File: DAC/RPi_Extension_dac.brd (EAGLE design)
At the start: 63 x 50 mm, 33 parts, among them U1 AD5360BSTZ, U2 ADR423ARZ

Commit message: updated pcbs
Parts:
- C1, C10, C12, C13, C15, C16, C2, C6, C8: value (none) -> 100nF
- C11, C14, C17, C3, C4, C5, C7, C9: value (none) -> 10uF
- R1, R2: value (none) -> 100k
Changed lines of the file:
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@@
 <attribute name="OC_FARNELL" value="unknown" x="29.25" y="4.55" size="1.778" layer="27" rot="R180" display="off"/>
 </element>
-<element name="C1" library="rcl" package="C0603" value="" x="17.55" y="28" rot="R270"/>
-<element name="C2" library="rcl" package="C0603" value="" x="25.8" y="28.35"/>
-<element name="C3" library="rcl" package="C1206" value="" x="16.15" y="31.3" rot="R180"/>
-<element name="C4" library="rcl" package="C1206" value="" x="26.35" y="31"/>
-<element name="C5" library="rcl" package="C1206" value="" x="9.1" y="22.75" rot="R90"/>
-<element name="C6" library="rcl" package="C0603" value="" x="11.7" y="22.2" rot="R90"/>
-<element name="C7" library="rcl" package="C1206" value="" x="35.1" y="13.85"/>
-<element name="C8" library="rcl" package="C0603" value="" x="29.9" y="13.65" rot="R270"/>
-<element name="C9" library="rcl" package="C1206" value="" x="9.1" y="16.25" rot="R270"/>
-<element name="C10" library="rcl" package="C0603" value="" x="11.7" y="16.8" rot="R270"/>
-<element name="C11" library="rcl" package="C1206" value="" x="35.1" y="16.9"/>
-<element name="C12" library="rcl" package="C0603" value="" x="29.95" y="17.1" rot="R90"/>
+<element name="C1" library="rcl" package="C0603" value="100nF" x="17.55" y="28" rot="R270"/>
+<element name="C2" library="rcl" package="C0603" value="100nF" x="25.8" y="28.35"/>
+<element name="C3" library="rcl" package="C1206" value="10uF" x="16.15" y="31.3" rot="R180"/>
+<element name="C4" library="rcl" package="C1206" value="10uF" x="26.35" y="31"/>
+<element name="C5" library="rcl" package="C1206" value="10uF" x="9.1" y="22.75" rot="R90"/>
+<element name="C6" library="rcl" package="C0603" value="100nF" x="11.7" y="22.2" rot="R90"/>
+<element name="C7" library="rcl" package="C1206" value="10uF" x="35.1" y="13.85"/>
+<element name="C8" library="rcl" package="C0603" value="100nF" x="29.9" y="13.65" rot="R270"/>
+<element name="C9" library="rcl" package="C1206" value="10uF" x="9.1" y="16.25" rot="R270"/>
+<element name="C10" library="rcl" package="C0603" value="100nF" x="11.7" y="16.8" rot="R270"/>
+<element name="C11" library="rcl" package="C1206" value="10uF" x="35.1" y="16.9"/>
+<element name="C12" library="rcl" package="C0603" value="100nF" x="29.95" y="17.1" rot="R90"/>
 <element name="SV3" library="con-lsta" package="FE08-2" value="" x="4.55" y="17.55" rot="R270">
 <attribute name="MPN" value="" x="4.55" y="17.55" size="1.778" layer="27" rot="R270" display="off"/>
@@
 <attribute name="VENDOR" value="Vendor" x="12.35" y="5.05" size="1.778" layer="27" display="off"/>
 </element>
-<element name="C13" library="rcl" package="C0603" value="" x="6.7" y="4.85" rot="R270"/>
-<element name="C14" library="rcl" package="C1206" value="" x="3.9" y="4.3" rot="R270"/>
-<element name="C15" library="rcl" package="C0603" value="" x="17.55" y="4.2" rot="R270"/>
-<element name="C16" library="rcl" package="C0603" value="" x="12.35" y="12.35" rot="R180"/>
-<element name="C17" library="rcl" package="C1206" value="" x="11.8" y="9.65" rot="R180"/>
+<element name="C13" library="rcl" package="C0603" value="100nF" x="6.7" y="4.85" rot="R270"/>
+<element name="C14" library="rcl" package="C1206" value="10uF" x="3.9" y="4.3" rot="R270"/>
+<element name="C15" library="rcl" package="C0603" value="100nF" x="17.55" y="4.2" rot="R270"/>
+<element name="C16" library="rcl" package="C0603" value="100nF" x="12.35" y="12.35" rot="R180"/>
+<element name="C17" library="rcl" package="C1206" value="10uF" x="11.8" y="9.65" rot="R180"/>
 <element name="SV2" library="con-lstb" package="MA08-2W" value="" x="51.35" y="4.55" rot="R180">
 <attribute name="MF" value="" x="51.35" y="4.55" size="1.778" layer="27" rot="R180" display="off"/>
@@
 <element name="SJ7" library="jumper" package="SJ" value="" x="8.45" y="35.1" rot="R270"/>
 <element name="SJ8" library="jumper" package="SJ" value="" x="4.55" y="35.1" rot="R270"/>
-<element name="R1" library="resistor" package="R0603" value="" x="12.2" y="25.05"/>
-<element name="R2" library="resistor" package="R0603" value="" x="12.2" y="27.6"/>
+<element name="R1" library="resistor" package="R0603" value="100k" x="12.2" y="25.05"/>
+<element name="R2" library="resistor" package="R0603" value="100k" x="12.2" y="27.6"/>
 </elements>
 <signals>

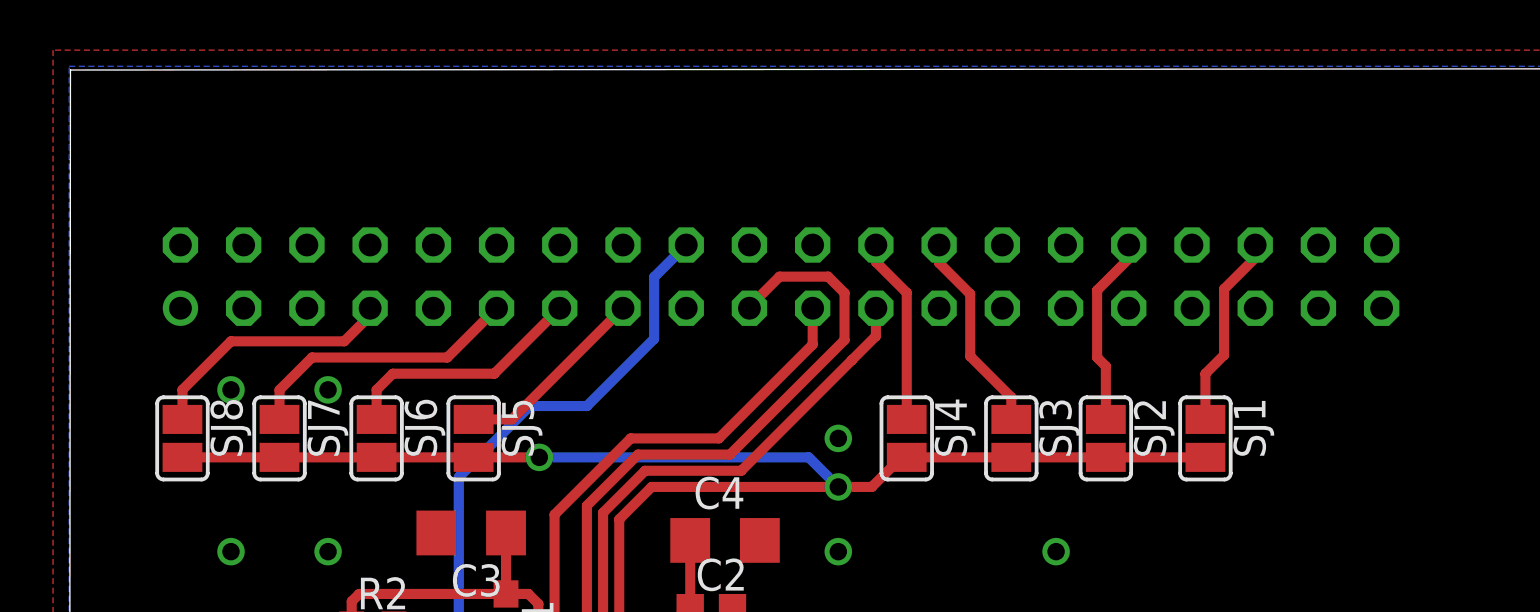
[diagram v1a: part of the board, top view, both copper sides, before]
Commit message: added additional id jumpers to adc and dac board
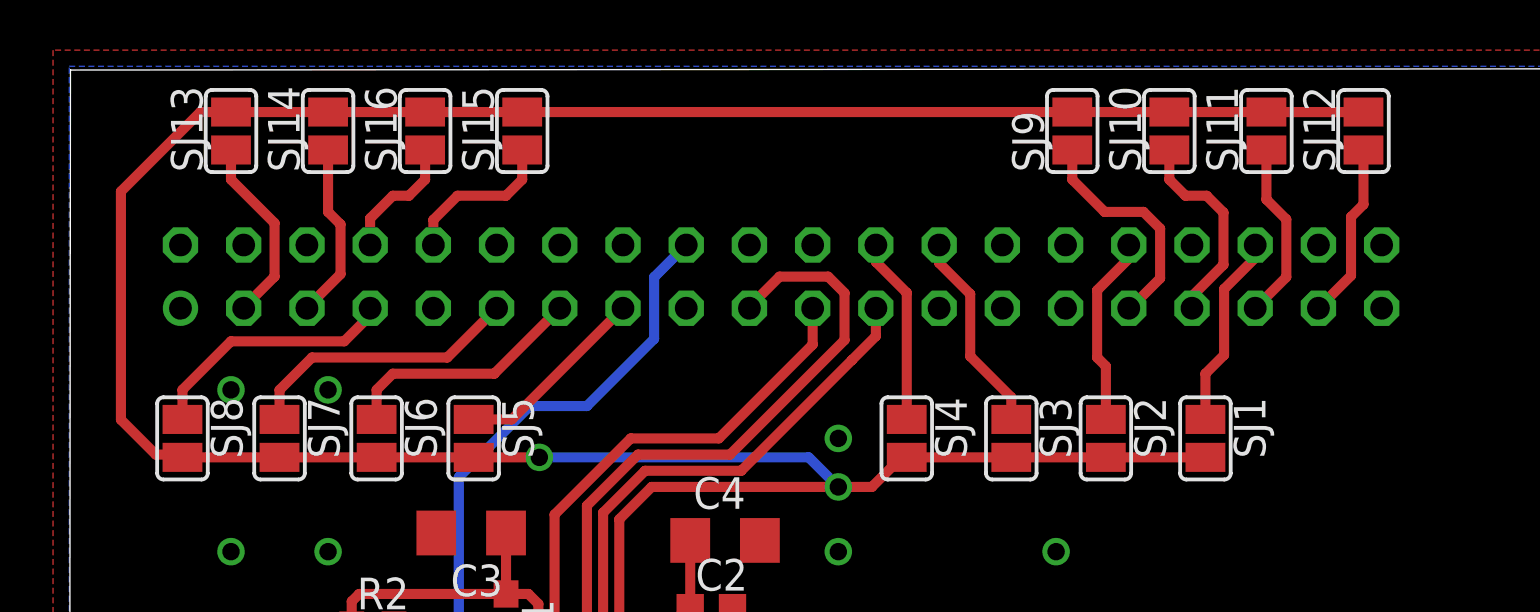
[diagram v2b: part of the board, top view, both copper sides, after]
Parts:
- added SJ10, SJ11, SJ12, SJ13, SJ14, SJ15, SJ16, SJ9: (no value), jumper:SJ
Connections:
- new net N$19: SJ9.1, SV5.31
- new net N$28: SJ10.1, SV5.33
- new net N$29: SJ11.1, SV5.35
- new net N$30: SJ12.1, SV5.37
- new net N$31: SJ13.1, SV5.3
- new net N$32: SJ14.1, SV5.5
- new net N$33: SJ16.1, SV5.8
- new net N$34: SJ15.1, SV5.10
- net SYNC: now also SJ10.2, SJ11.2, SJ12.2, SJ13.2, SJ14.2, SJ15.2, SJ16.2, SJ9.2
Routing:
- net SYNC: track 58.8 -> 126.2 mm
- net N$19: track 0.00 -> 9.29 mm
- net N$28: track 0.00 -> 8.28 mm
- net N$31: track 0.00 -> 7.60 mm
- net N$29: track 0.00 -> 7.21 mm
- net N$32: track 0.00 -> 7.12 mm
- net N$30: track 0.00 -> 7.11 mm
- net N$34: track 0.00 -> 6.44 mm
- net N$33: track 0.00 -> 5.11 mm
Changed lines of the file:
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@@
 <element name="R1" library="resistor" package="R0603" value="100k" x="12.2" y="25.05"/>
 <element name="R2" library="resistor" package="R0603" value="100k" x="12.2" y="27.6"/>
+<element name="SJ9" library="jumper" package="SJ" value="" x="40.3" y="47.45" rot="R90"/>
+<element name="SJ10" library="jumper" package="SJ" value="" x="44.2" y="47.45" rot="R90"/>
+<element name="SJ11" library="jumper" package="SJ" value="" x="48.1" y="47.45" rot="R90"/>
+<element name="SJ12" library="jumper" package="SJ" value="" x="52" y="47.45" rot="R90"/>
+<element name="SJ13" library="jumper" package="SJ" value="" x="6.5" y="47.45" rot="R90"/>
+<element name="SJ14" library="jumper" package="SJ" value="" x="10.4" y="47.45" rot="R90"/>
+<element name="SJ15" library="jumper" package="SJ" value="" x="18.2" y="47.45" rot="R90"/>
+<element name="SJ16" library="jumper" package="SJ" value="" x="14.3" y="47.45" rot="R90"/>
 </elements>
 <signals>
@@
 <wire x1="33.438" y1="34.338" x2="32.25" y2="33.15" width="0.4064" layer="1"/>
 <wire x1="32.25" y1="33.15" x2="30.9" y2="33.15" width="0.4064" layer="1"/>
+<contactref element="SJ9" pad="2"/>
+<contactref element="SJ10" pad="2"/>
+<contactref element="SJ11" pad="2"/>
+<contactref element="SJ12" pad="2"/>
+<contactref element="SJ15" pad="2"/>
+<contactref element="SJ16" pad="2"/>
+<contactref element="SJ14" pad="2"/>
+<contactref element="SJ13" pad="2"/>
+<wire x1="52" y1="48.212" x2="48.1" y2="48.212" width="0.4064" layer="1"/>
+<wire x1="52" y1="48.212" x2="44.2" y2="48.212" width="0.4064" layer="1"/>
+<wire x1="18.2" y1="48.212" x2="40.3" y2="48.212" width="0.4064" layer="1"/>
+<wire x1="40.3" y1="48.212" x2="44.2" y2="48.212" width="0.4064" layer="1"/>
+<wire x1="18.2" y1="48.212" x2="14.3" y2="48.212" width="0.4064" layer="1"/>
+<wire x1="6.5" y1="48.212" x2="5.268409375" y2="48.212" width="0.4064" layer="1"/>
+<wire x1="5.268409375" y1="48.212" x2="2.077546875" y2="45.0211375" width="0.4064" layer="1"/>
+<wire x1="2.077546875" y1="45.0211375" x2="2.077546875" y2="35.851053125" width="0.4064" layer="1"/>
+<wire x1="2.077546875" y1="35.851053125" x2="3.4786" y2="34.45" width="0.4064" layer="1"/>
+<wire x1="3.4786" y1="34.45" x2="4.438" y2="34.45" width="0.4064" layer="1"/>
+<wire x1="4.438" y1="34.45" x2="4.55" y2="34.338" width="0.4064" layer="1"/>
+<wire x1="6.5" y1="48.212" x2="10.4" y2="48.212" width="0.4064" layer="1"/>
+<wire x1="10.4" y1="48.212" x2="14.3" y2="48.212" width="0.4064" layer="1"/>
 </signal>
 <signal name="N$20">
@@
 <wire x1="15.65" y1="22.85" x2="15.65" y2="25.35" width="0.4064" layer="1"/>
 </signal>
+<signal name="N$19">
+<contactref element="SV5" pad="31"/>
+<contactref element="SJ9" pad="1"/>
+<wire x1="42.57" y1="40.33" x2="42.63" y2="40.33" width="0.4064" layer="1"/>
+<wire x1="42.63" y1="40.33" x2="43.830259375" y2="41.530259375" width="0.4064" layer="1"/>
+<wire x1="43.830259375" y1="41.530259375" x2="43.83025625" y2="43.531503125" width="0.4064" layer="1"/>
+<wire x1="43.83025625" y1="43.531503125" x2="43.161759375" y2="44.2" width="0.4064" layer="1"/>
+<wire x1="43.161759375" y1="44.2" x2="41.6" y2="44.2" width="0.4064" layer="1"/>
+<wire x1="41.6" y1="44.2" x2="40.3" y2="45.5" width="0.4064" layer="1"/>
+<wire x1="40.3" y1="45.5" x2="40.3" y2="46.688" width="0.4064" layer="1"/>
+</signal>
+<signal name="N$28">
+<contactref element="SV5" pad="33"/>
+<contactref element="SJ10" pad="1"/>
+<wire x1="44.2" y1="46.688" x2="44.2" y2="45.5" width="0.4064" layer="1"/>
+<wire x1="44.2" y1="45.5" x2="44.85" y2="44.85" width="0.4064" layer="1"/>
+<wire x1="44.85" y1="44.85" x2="45.7" y2="44.85" width="0.4064" layer="1"/>
+<wire x1="45.7" y1="44.85" x2="46.374953125" y2="44.175046875" width="0.4064" layer="1"/>
+<wire x1="45.11" y1="40.33" x2="45.11" y2="40.81" width="0.4064" layer="1"/>
+<wire x1="46.374953125" y1="44.175046875" x2="46.374953125" y2="42.074953125" width="0.4064" layer="1"/>
+<wire x1="46.374953125" y1="42.074953125" x2="45.11" y2="40.81" width="0.4064" layer="1"/>
+</signal>
+<signal name="N$29">
+<contactref element="SV5" pad="35"/>
+<contactref element="SJ11" pad="1"/>
+<wire x1="48.1" y1="46.688" x2="48.1" y2="44.7" width="0.4064" layer="1"/>
+<wire x1="48.1" y1="44.7" x2="48.9" y2="43.9" width="0.4064" layer="1"/>
+<wire x1="48.9" y1="43.9" x2="48.9" y2="41.58" width="0.4064" layer="1"/>
+<wire x1="48.9" y1="41.58" x2="47.65" y2="40.33" width="0.4064" layer="1"/>
+</signal>
+<signal name="N$30">
+<contactref element="SV5" pad="37"/>
+<contactref element="SJ12" pad="1"/>
+<wire x1="52" y1="46.688" x2="52" y2="44.5" width="0.4064" layer="1"/>
+<wire x1="52" y1="44.5" x2="51.5" y2="44" width="0.4064" layer="1"/>
+<wire x1="51.5" y1="44" x2="51.5" y2="41.64" width="0.4064" layer="1"/>
+<wire x1="51.5" y1="41.64" x2="50.19" y2="40.33" width="0.4064" layer="1"/>
+</signal>
+<signal name="N$31">
+<contactref element="SV5" pad="3"/>
+<contactref element="SJ13" pad="1"/>
+<wire x1="7.01" y1="40.33" x2="7.01" y2="40.36" width="0.4064" layer="1"/>
+<wire x1="7.01" y1="40.36" x2="8.25" y2="41.6" width="0.4064" layer="1"/>
+<wire x1="8.25" y1="41.6" x2="8.25" y2="43.75" width="0.4064" layer="1"/>
+<wire x1="8.25" y1="43.75" x2="6.5" y2="45.5" width="0.4064" layer="1"/>
+<wire x1="6.5" y1="46.688" x2="6.5" y2="45.5" width="0.4064" layer="1"/>
+</signal>
+<signal name="N$32">
+<contactref element="SV5" pad="5"/>
+<contactref element="SJ14" pad="1"/>
+<wire x1="9.55" y1="40.33" x2="9.55" y2="40.35" width="0.4064" layer="1"/>
+<wire x1="9.55" y1="40.35" x2="10.9" y2="41.7" width="0.4064" layer="1"/>
+<wire x1="10.9" y1="41.7" x2="10.9" y2="43.7" width="0.4064" layer="1"/>
+<wire x1="10.9" y1="43.7" x2="10.4" y2="44.2" width="0.4064" layer="1"/>
+<wire x1="10.4" y1="44.2" x2="10.4" y2="46.688" width="0.4064" layer="1"/>
+</signal>
+<signal name="N$33">
+<contactref element="SV5" pad="8"/>
+<contactref element="SJ16" pad="1"/>
+<wire x1="12.09" y1="42.87" x2="12.09" y2="43.94" width="0.4064" layer="1"/>
+<wire x1="12.09" y1="43.94" x2="13" y2="44.85" width="0.4064" layer="1"/>
+<wire x1="13" y1="44.85" x2="13.65" y2="44.85" width="0.4064" layer="1"/>
+<wire x1="13.65" y1="44.85" x2="14.3" y2="45.5" width="0.4064" layer="1"/>
+<wire x1="14.3" y1="45.5" x2="14.3" y2="46.688" width="0.4064" layer="1"/>
+</signal>
+<signal name="N$34">
+<contactref element="SV5" pad="10"/>
+<contactref element="SJ15" pad="1"/>
+<wire x1="14.63" y1="42.87" x2="14.63" y2="43.88" width="0.4064" layer="1"/>
+<wire x1="14.63" y1="43.88" x2="15.6" y2="44.85" width="0.4064" layer="1"/>
+<wire x1="15.6" y1="44.85" x2="17.55" y2="44.85" width="0.4064" layer="1"/>
+<wire x1="17.55" y1="44.85" x2="18.2" y2="45.5" width="0.4064" layer="1"/>
+<wire x1="18.2" y1="45.5" x2="18.2" y2="46.688" width="0.4064" layer="1"/>
+</signal>
 </signals>
